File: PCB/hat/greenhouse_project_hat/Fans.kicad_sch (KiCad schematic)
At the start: 28 parts, among them Q9 DMN6040SVT-7

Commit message: Updated PCB files
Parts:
- removed D? (x4): 1N4007, Diode_SMD:D_2512_6332Metric_Pad1.52x3.35mm_HandSolder, symbol Diode:1N4007
- removed TP1 (x3): TestPoint, TestPoint:TestPoint_Pad_D2.0mm, symbol Connector:TestPoint
- added D11, D12, D13, D14: RS2MA-13-F, DIOM5226X230N, symbol SamacSys_Parts:RS2MA-13-F
- added TP1 (x3): TestPoint, TestPoint:TestPoint_Pad_D2.0mm, symbol Connector:TestPoint
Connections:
- net Fan1+: now also D11.1
- net Fan1-: now also D11.2
- net Fan2+: now also D12.1
- net Fan2-: now also D12.2, TP1.1
- net Fan3+: now also D13.1
- net Fan3-: now also D13.2, TP1.1
- net Fan4+: now also D14.1
- net Fan4-: now also D14.2, TP1.1
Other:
- moved on the sheet: J?, JP6, TP1

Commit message: Update: hat V5.0
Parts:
- JP4, JP5, JP6, JP7, TP1: now left out of the parts list
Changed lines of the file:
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@@
   (title_block
     (title "Greenhouse project FRDM-KL25Z hat")
-    (date "16-03-2023")
-    (rev "v4.0")
+    (date "18-03-2023")
+    (rev "v5.0")
     (company "OnlyPlants")
     (comment 1 "Author: Emiel Visser")
@@
   )
   (symbol (lib_id "Jumper:Jumper_3_Bridged12") (at 55.88 30.48 0) (mirror y) (unit 1)
-    (in_bom yes) (on_board yes) (dnp no)
+    (in_bom no) (on_board yes) (dnp no)
     (property "Reference" "JP4" (at 55.88 25.4 0)
       (effects (font (size 1.27 1.27)))
@@
   )
   (symbol (lib_id "Connector:TestPoint") (at 35.56 143.51 90) (unit 1)
-    (in_bom yes) (on_board yes) (dnp no) (fields_autoplaced)
+    (in_bom no) (on_board yes) (dnp no) (fields_autoplaced)
     (property "Reference" "TP1" (at 32.258 138.43 90)
       (effects (font (size 1.27 1.27)))
@@
   )
   (symbol (lib_id "Jumper:Jumper_3_Bridged12") (at 123.19 111.76 0) (mirror y) (unit 1)
-    (in_bom yes) (on_board yes) (dnp no)
+    (in_bom no) (on_board yes) (dnp no)
     (property "Reference" "JP7" (at 123.19 106.68 0)
       (effects (font (size 1.27 1.27)))
@@
   )
   (symbol (lib_id "Connector:TestPoint") (at 101.6 142.24 90) (unit 1)
-    (in_bom yes) (on_board yes) (dnp no) (fields_autoplaced)
+    (in_bom no) (on_board yes) (dnp no) (fields_autoplaced)
     (property "Reference" "TP1" (at 98.298 137.16 90)
       (effects (font (size 1.27 1.27)))
@@
   )
   (symbol (lib_id "Connector:TestPoint") (at 52.07 40.64 90) (unit 1)
-    (in_bom yes) (on_board yes) (dnp no) (fields_autoplaced)
+    (in_bom no) (on_board yes) (dnp no) (fields_autoplaced)
     (property "Reference" "TP1" (at 48.768 35.56 90)
       (effects (font (size 1.27 1.27)))
@@
   )
   (symbol (lib_id "Connector:TestPoint") (at 34.29 60.96 90) (unit 1)
-    (in_bom yes) (on_board yes) (dnp no) (fields_autoplaced)
+    (in_bom no) (on_board yes) (dnp no) (fields_autoplaced)
     (property "Reference" "TP1" (at 30.988 55.88 90)
       (effects (font (size 1.27 1.27)))
@@
   )
   (symbol (lib_id "Jumper:Jumper_3_Bridged12") (at 121.92 30.48 0) (mirror y) (unit 1)
-    (in_bom yes) (on_board yes) (dnp no)
+    (in_bom no) (on_board yes) (dnp no)
     (property "Reference" "JP6" (at 121.92 25.4 0)
       (effects (font (size 1.27 1.27)))
@@
   )
   (symbol (lib_id "Connector:TestPoint") (at 100.33 59.69 90) (unit 1)
-    (in_bom yes) (on_board yes) (dnp no) (fields_autoplaced)
+    (in_bom no) (on_board yes) (dnp no) (fields_autoplaced)
     (property "Reference" "TP1" (at 97.028 54.61 90)
       (effects (font (size 1.27 1.27)))
@@
   )
   (symbol (lib_id "Jumper:Jumper_3_Bridged12") (at 57.15 111.76 0) (mirror y) (unit 1)
-    (in_bom yes) (on_board yes) (dnp no)
+    (in_bom no) (on_board yes) (dnp no)
     (property "Reference" "JP5" (at 57.15 106.68 0)
       (effects (font (size 1.27 1.27)))
@@
   )
   (symbol (lib_id "Connector:TestPoint") (at 118.11 40.64 90) (unit 1)
-    (in_bom yes) (on_board yes) (dnp no)
+    (in_bom no) (on_board yes) (dnp no)
     (property "Reference" "TP1" (at 114.3 35.56 90)
       (effects (font (size 1.27 1.27)))
@@
   )
   (symbol (lib_id "Connector:TestPoint") (at 54.61 121.92 90) (unit 1)
-    (in_bom yes) (on_board yes) (dnp no) (fields_autoplaced)
+    (in_bom no) (on_board yes) (dnp no) (fields_autoplaced)
     (property "Reference" "TP1" (at 51.308 116.84 90)
       (effects (font (size 1.27 1.27)))
@@
   )
   (symbol (lib_id "Connector:TestPoint") (at 120.65 121.92 90) (unit 1)
-    (in_bom yes) (on_board yes) (dnp no) (fields_autoplaced)
+    (in_bom no) (on_board yes) (dnp no) (fields_autoplaced)
     (property "Reference" "TP1" (at 117.348 116.84 90)
       (effects (font (size 1.27 1.27)))

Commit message: First production version
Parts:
- D10: renamed from D12; footprint DIOM5226X230N -> SamacSys_Parts:DIOM5226X230N
- D11: renamed from D13; footprint DIOM5226X230N -> SamacSys_Parts:DIOM5226X230N
- D12: renamed from D14; footprint DIOM5226X230N -> SamacSys_Parts:DIOM5226X230N
- D9: renamed from D11; footprint DIOM5226X230N -> SamacSys_Parts:DIOM5226X230N
- JP4, JP5, JP6, JP7, TP1: now in the parts list
- Q9: footprint SOT95P280X90-6N -> SamacSys_Parts:SOT95P280X90-6N

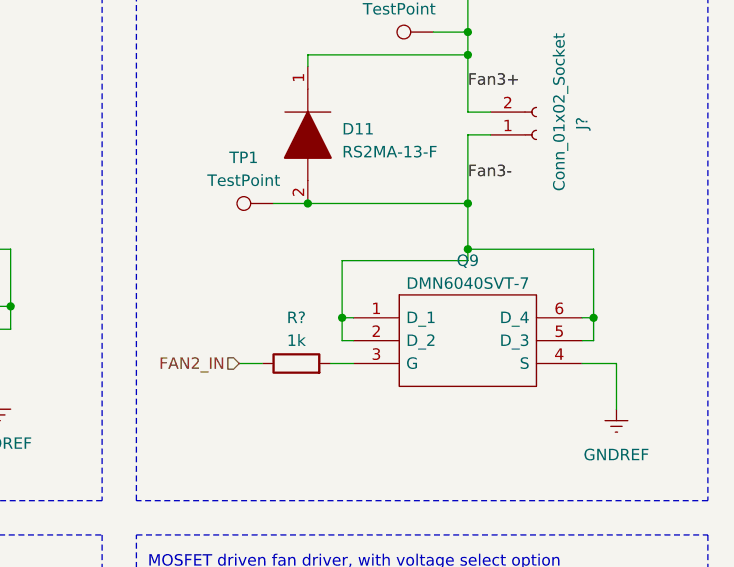
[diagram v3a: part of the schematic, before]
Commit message: Uploaded finals
Pushed the final versions of the microcontroller code, Nodered code, PCB and CAD files to the repository
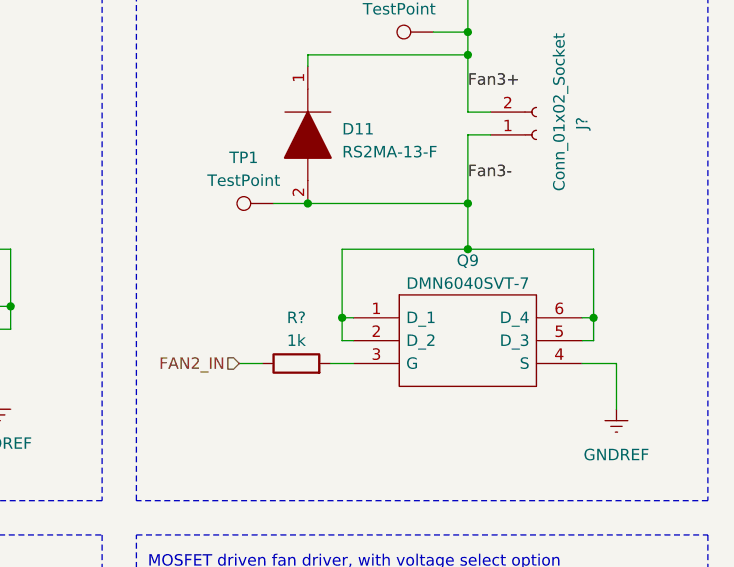
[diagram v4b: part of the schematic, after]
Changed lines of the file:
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@@
-    (stroke (width 0) (type default))
-  )
-  (wire (pts (xy 121.92 66.04) (xy 121.92 64.77))
     (stroke (width 0) (type default))
   )
@@
     (stroke (width 0) (type default))
   )
-  (wire (pts (xy 107.95 66.04) (xy 107.95 72.39))
+  (wire (pts (xy 107.95 64.77) (xy 107.95 72.39))
     (stroke (width 0) (type default))
   )
@@
     (stroke (width 0) (type default))
   )
-  (wire (pts (xy 121.92 66.04) (xy 107.95 66.04))
+  (wire (pts (xy 121.92 64.77) (xy 107.95 64.77))
     (stroke (width 0) (type default))
   )
